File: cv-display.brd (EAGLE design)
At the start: 45.1 x 130.8 mm, 92 parts, among them IC1 TL072JD, IC10 VOLTMETER, IC2 TL072JD, IC3 TL072JD, IC4 TL072JD, IC5 TL072JD, IC6 TL072JD, IC7 VOLTMETER, IC8 VOLTMETER, IC9 VOLTMETER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

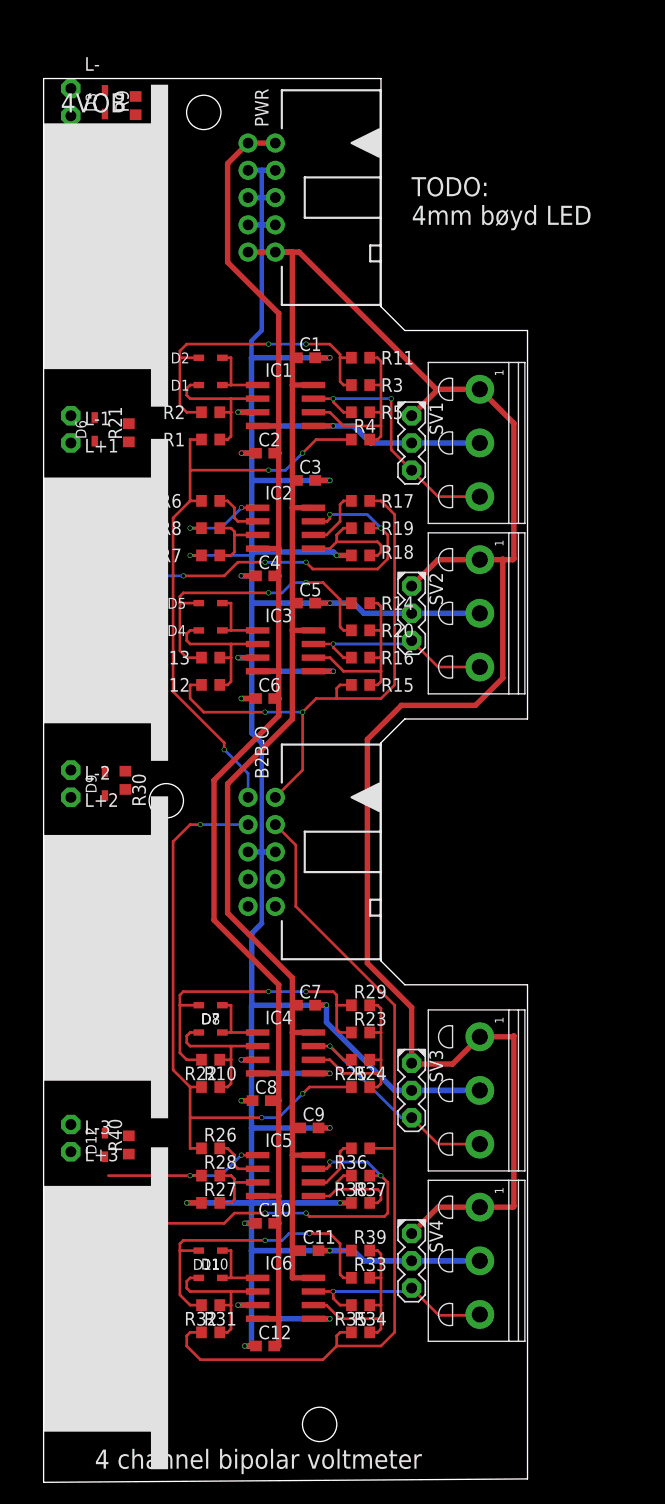
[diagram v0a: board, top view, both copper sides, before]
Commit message: No airwires, just led placements left
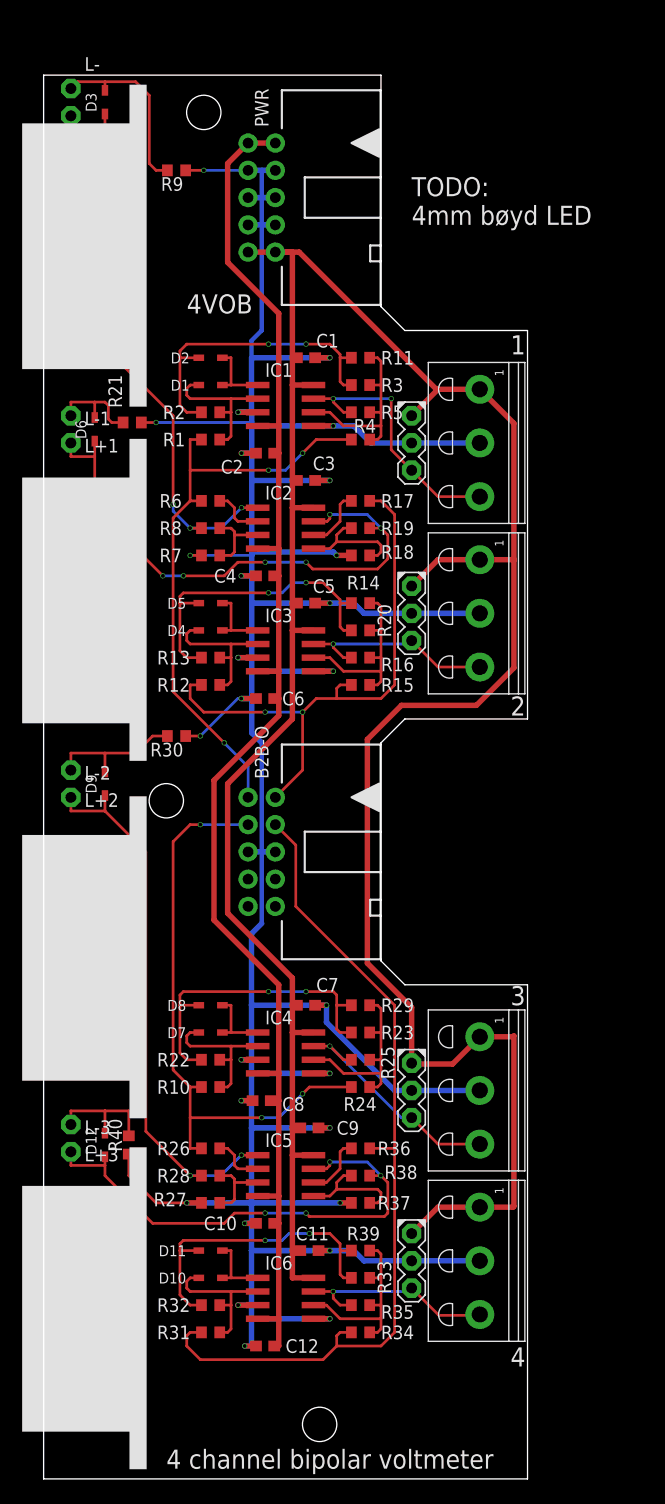
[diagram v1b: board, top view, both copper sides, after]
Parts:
- moved R9 7.13 mm to (12.4, 121.9), turned to 180 degrees
- moved R30 6.30 mm to (12.4, 69.2), turned to 180 degrees
- moved IC10 2.00 mm to (-2.00, 15.9)
- moved IC7 2.00 mm to (-2.00, 114.9)
- moved IC8 2.00 mm to (-2.00, 81.9)
- moved IC9 2.00 mm to (-2.00, 48.6)
- moved R21 1.00 mm to (8.26, 98.4), turned to 180 degrees
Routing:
- net N$6: track 8.13 -> 54.5 mm, vias 2 -> 3
- net N$23: track 15.8 -> 51.3 mm
- net GND: track 328.5 -> 359.7 mm, vias 24 -> 27
- net N$19: track 33.6 -> 52.3 mm
- net N$12: track 0.00 -> 17.2 mm
- net N$24: track 0.00 -> 13.0 mm
- net N$31: track 34.7 -> 47.2 mm
- net N$32: track 0.00 -> 11.1 mm
- net N$20: track 0.00 -> 9.11 mm
- net +12V: track 269.8 -> 270.6 mm
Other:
- outline, holes or cut-outs redrawn
- board text added: "1"
- board text added: "2"
- board text added: "3"
- board text added: "4"

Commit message: Fixed leds and display sizes
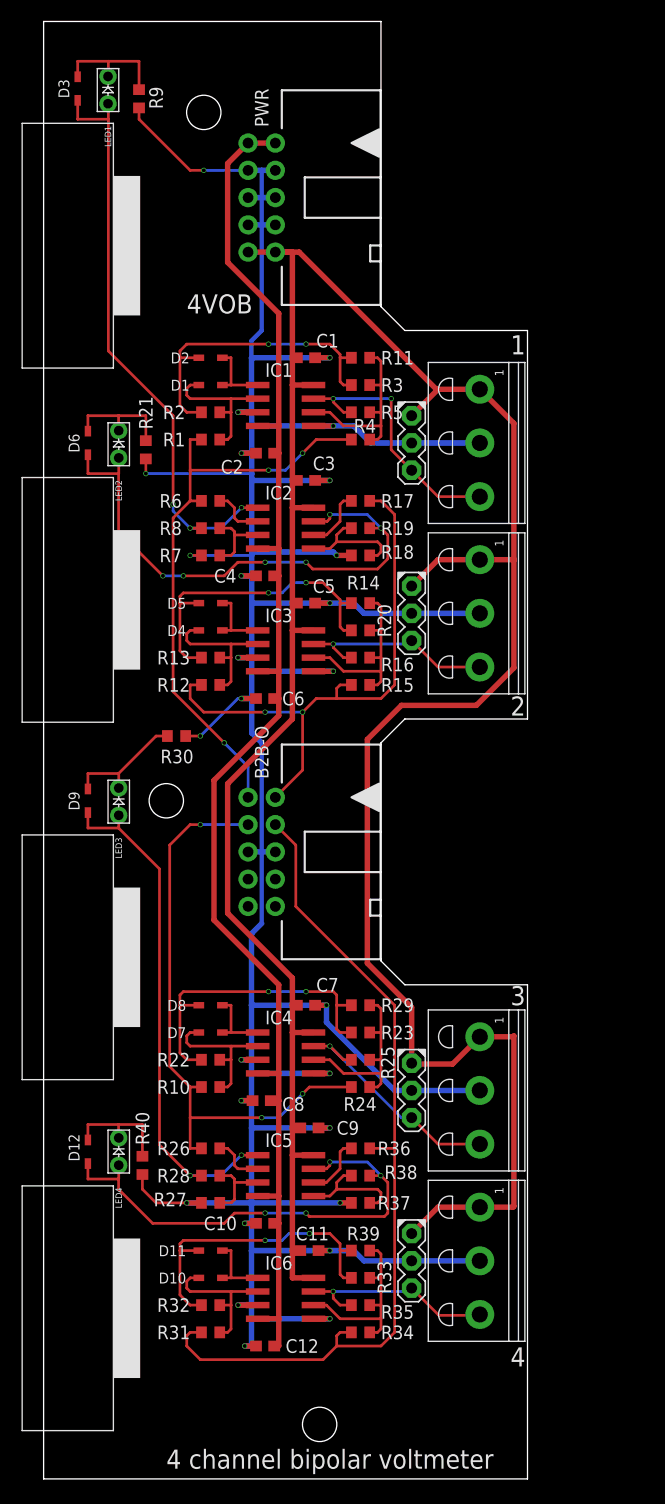
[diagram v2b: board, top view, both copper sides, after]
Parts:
- removed L+, L+1, L+2, L+3, L-, L-1, L-2, L-3: (no value), joakim:MA01N-1J
- added LED1, LED2, LED3, LED4: (no value), joakim-old:LED2X4-J
- moved R9 7.53 mm to (8.89, 128.6), turned to 90 degrees
- moved R21 2.84 mm to (9.53, 95.9), turned to 90 degrees
- moved D3 2.84 mm to (3.17, 129.5)
- moved R40 2.29 mm to (9.21, 29.2)
- moved D9 2.25 mm to (4.13, 63.2)
- moved D12 1.71 mm to (4.13, 30.5)
- moved D6 1.42 mm to (4.13, 96.5)
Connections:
- net N$12: now also LED1.CATHODE; no longer L-.1
- net N$19: now also LED2.ANODE; no longer L+1.1
- net N$20: now also LED2.CATHODE; no longer L-1.1
- net N$23: now also LED3.ANODE; no longer L+2.1
- net N$24: now also LED3.CATHODE; no longer L-2.1
- net N$31: now also LED4.ANODE; no longer L+3.1
- net N$32: now also LED4.CATHODE; no longer L-3.1
- net N$6: now also LED1.ANODE; no longer L+.1
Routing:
- net N$12: track 17.2 -> 11.2 mm
- net GND: track 359.7 -> 365.6 mm
- net N$23: track 51.3 -> 48.8 mm
- net N$31: track 47.2 -> 45.7 mm
- net N$20: track 9.11 -> 10.6 mm
- net N$19: track 52.3 -> 50.9 mm
- net N$24: track 13.0 -> 11.7 mm
- net N$6: track 54.5 -> 55.5 mm
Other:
- board size 45.1 x 130.8 mm -> 45.1 x 135.8 mm
- board text removed: "TODO: 4mm bøyd LED"

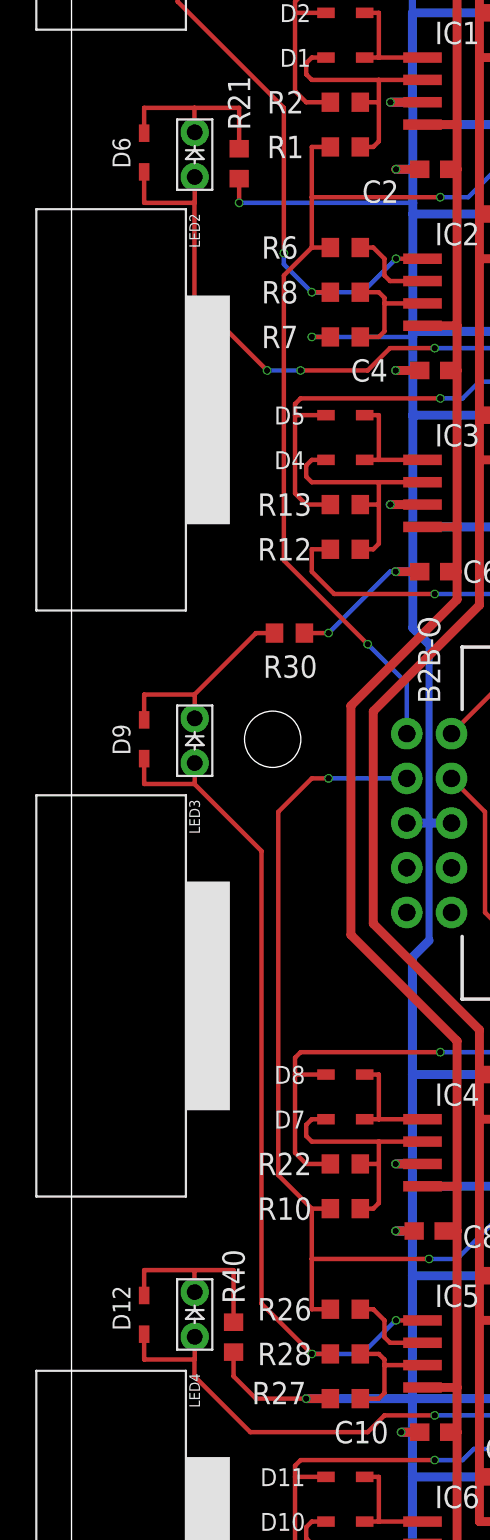
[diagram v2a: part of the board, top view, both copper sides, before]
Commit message: Wrong led positions
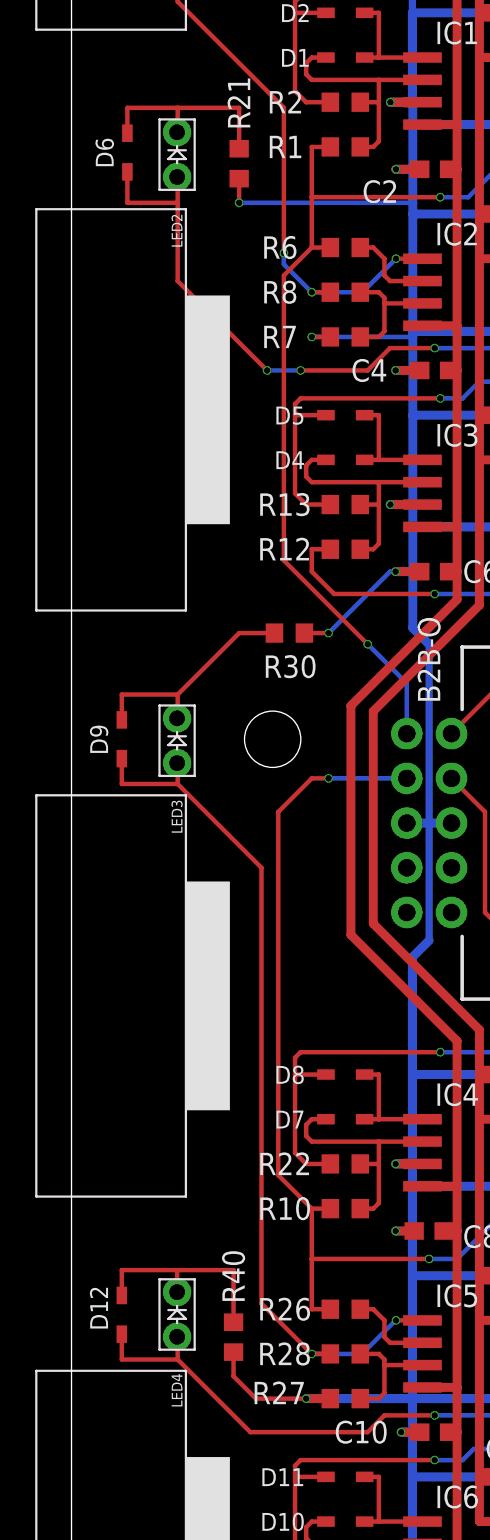
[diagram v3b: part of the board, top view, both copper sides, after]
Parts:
- moved D12 1.27 mm to (2.86, 30.5)
- moved D9 1.27 mm to (2.86, 63.2)
- moved LED2 1.00 mm to (6.00, 96.4)
- moved LED3 1.00 mm to (6.00, 63.1)
- moved LED4 1.00 mm to (6.00, 30.5)
- moved D6 0.95 mm to (3.17, 96.5)
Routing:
- net N$24: track 11.7 -> 12.9 mm
- net N$32: track 10.7 -> 12.0 mm
- net N$20: track 10.6 -> 11.5 mm
- net N$23: track 48.8 -> 49.5 mm
- net N$31: track 45.7 -> 46.4 mm

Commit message: Sent to production
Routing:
- net +12V: track 270.6 -> 267.5 mm
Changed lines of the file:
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@@
 <wire x1="25.1425" y1="41.5925" x2="23.1775" y2="41.5925" width="0.508" layer="1"/>
 <wire x1="23.5975" y1="44.1325" x2="23.1775" y2="44.1325" width="0.508" layer="1"/>
-<wire x1="21.59" y1="114.3" x2="23.1775" y2="114.3" width="0.508" layer="1"/>
 <wire x1="19.05" y1="114.3" x2="21.59" y2="114.3" width="0.508" layer="1"/>
 <wire x1="23.1775" y1="101.9175" x2="23.1775" y2="104.4575" width="0.508" layer="1"/>
-<wire x1="23.1775" y1="104.4575" x2="23.1775" y2="114.3" width="0.508" layer="1"/>
+<wire x1="23.1775" y1="104.4575" x2="23.1775" y2="112.7125" width="0.508" layer="1"/>
 <wire x1="43.815" y1="41.275" x2="43.815" y2="25.4" width="0.508" layer="1"/>
 <wire x1="43.815" y1="25.4" x2="43.735" y2="25.32" width="0.508" layer="1"/>
@@
 <wire x1="43.815" y1="98.345" x2="40.64" y2="101.52" width="0.508" layer="1"/>
 <wire x1="36.75" y1="101.52" x2="36.5925" y2="101.52" width="0.508" layer="1"/>
-<wire x1="36.5925" y1="101.52" x2="23.8125" y2="114.3" width="0.508" layer="1"/>
-<wire x1="21.59" y1="114.3" x2="23.8125" y2="114.3" width="0.508" layer="1"/>
+<wire x1="36.5925" y1="101.52" x2="25.4" y2="112.7125" width="0.508" layer="1"/>
+<wire x1="25.4" y1="112.7125" x2="23.1775" y2="112.7125" width="0.508" layer="1"/>
+<wire x1="21.59" y1="114.3" x2="23.1775" y2="112.7125" width="0.508" layer="1"/>
 <wire x1="34.37" y1="38.655" x2="34.29" y2="38.735" width="0.508" layer="1"/>
 <wire x1="38.1" y1="38.655" x2="34.37" y2="38.655" width="0.508" layer="1"/>
